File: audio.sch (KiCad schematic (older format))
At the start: 25 parts, among them U1 UDA1334A, U2 LM386, U3 LM386

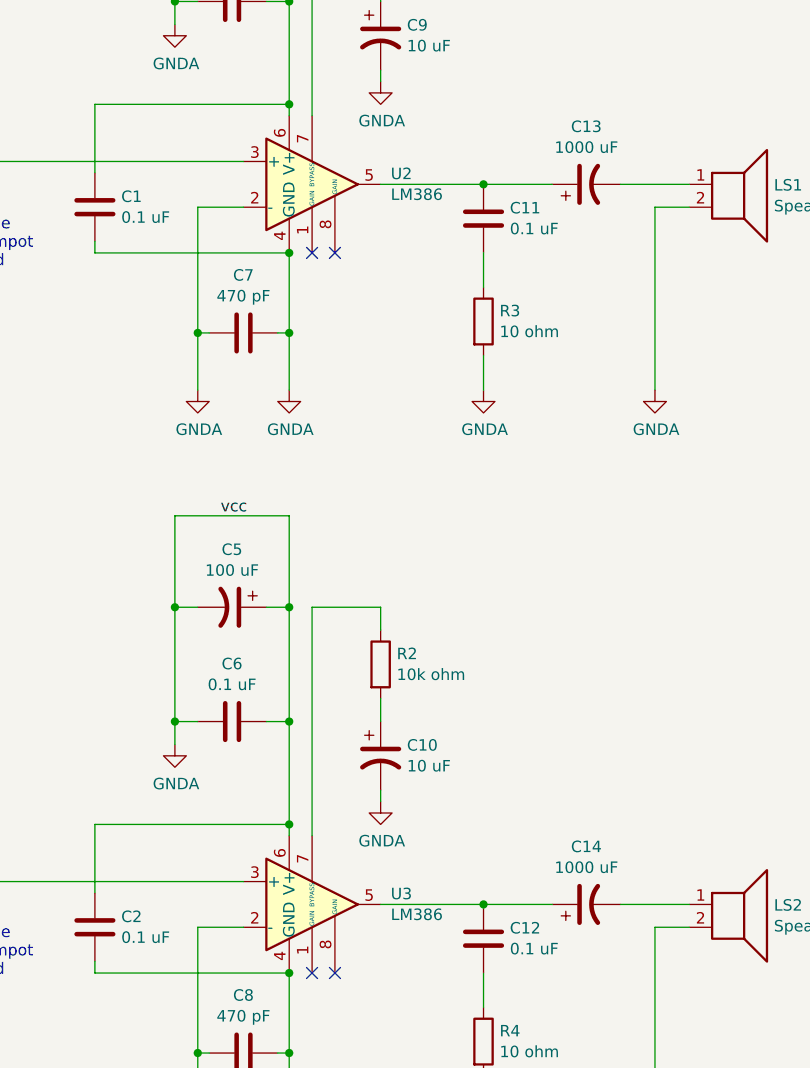
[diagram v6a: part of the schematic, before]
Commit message: Add side-actuated tactile switch footprint.
Made MJTP1236 footprint using datasheet reference in FreeCAD. Imported
to KiCAD using StepUp. Couldn't figure out how to name the through hole
layer properly so I used SMD pads and manually converted them to through
holes inside KiCAD.
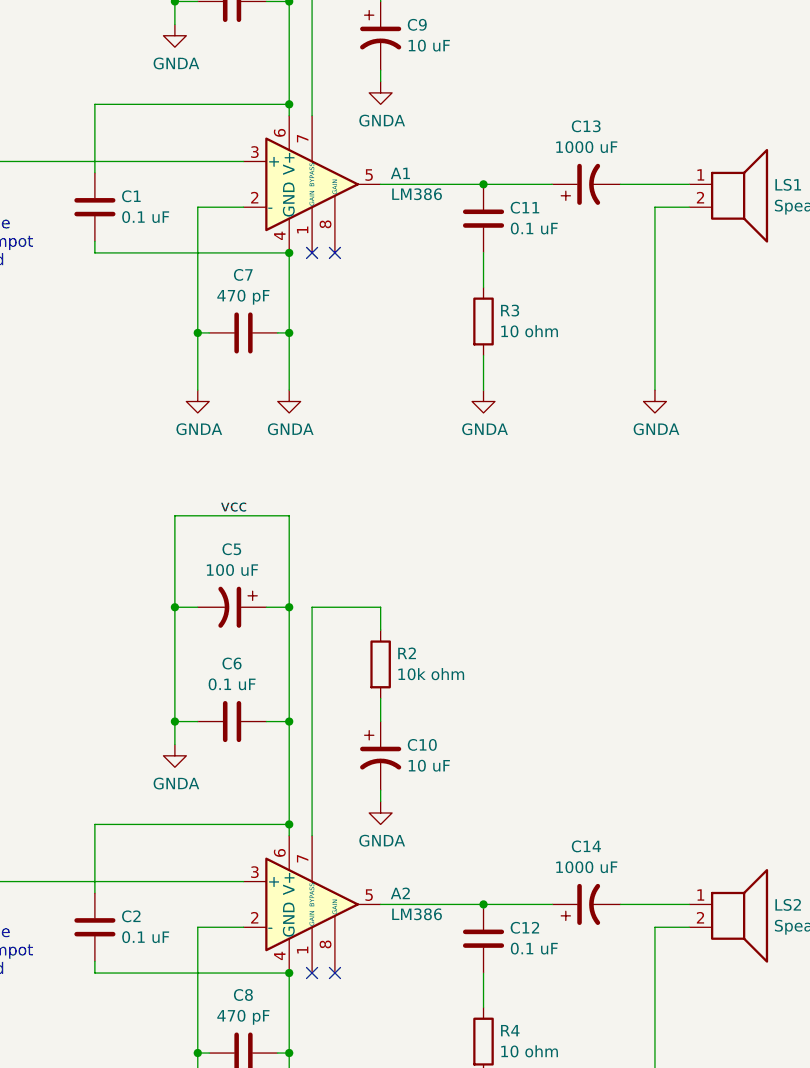
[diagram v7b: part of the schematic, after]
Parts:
- A1: renamed from U2; footprint (none) -> Package_DIP:DIP-8_W7.62mm
- A2: renamed from U3; footprint (none) -> Package_DIP:DIP-8_W7.62mm
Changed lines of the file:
@@
 $EndDescr
 $Comp
-L Amplifier_Audio:LM386 U2
+L Amplifier_Audio:LM386 A1
 U 1 1 60687AB3
 P 6600 2350
-F 0 "U2" H 6944 2396 50  0000 L CNN
+F 0 "A1" H 6944 2396 50  0000 L CNN
 F 1 "LM386" H 6944 2305 50  0000 L CNN
-F 2 "" H 6700 2450 50  0001 C CNN
+F 2 "Package_DIP:DIP-8_W7.62mm" H 6700 2450 50  0001 C CNN
 F 3 "http://www.ti.com/lit/ds/symlink/lm386.pdf" H 6800 2550 50  0001 C CNN
 	1    6600 2350
@@
 	4800 2250 6300 2250
 $Comp
-L Amplifier_Audio:LM386 U3
+L Amplifier_Audio:LM386 A2
 U 1 1 606DD65F
 P 6600 5500
-F 0 "U3" H 6944 5546 50  0000 L CNN
+F 0 "A2" H 6944 5546 50  0000 L CNN
 F 1 "LM386" H 6944 5455 50  0000 L CNN
-F 2 "" H 6700 5600 50  0001 C CNN
+F 2 "Package_DIP:DIP-8_W7.62mm" H 6700 5600 50  0001 C CNN
 F 3 "http://www.ti.com/lit/ds/symlink/lm386.pdf" H 6800 5700 50  0001 C CNN
 	1    6600 5500

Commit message: Download speaker footprint off SnapEDA and mod it.
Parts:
- LS1, LS2: footprint (none) -> SMS-1308MS-2-R:SMS-1308MS-2-R
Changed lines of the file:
@@
 F 0 "LS1" H 8620 2346 50  0000 L CNN
 F 1 "Speaker" H 8620 2255 50  0000 L CNN
-F 2 "" H 8450 2150 50  0001 C CNN
+F 2 "SMS-1308MS-2-R:SMS-1308MS-2-R" H 8450 2150 50  0001 C CNN
 F 3 "~" H 8440 2300 50  0001 C CNN
 	1    8450 2350
@@
 F 0 "LS2" H 8620 5496 50  0000 L CNN
 F 1 "Speaker" H 8620 5405 50  0000 L CNN
-F 2 "" H 8450 5300 50  0001 C CNN
+F 2 "SMS-1308MS-2-R:SMS-1308MS-2-R" H 8450 5300 50  0001 C CNN
 F 3 "~" H 8440 5450 50  0001 C CNN
 	1    8450 5500
